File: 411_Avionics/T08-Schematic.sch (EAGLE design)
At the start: 19 parts, among them IC1 BQ24022, U1 USB_In, U3 LSM9DS0

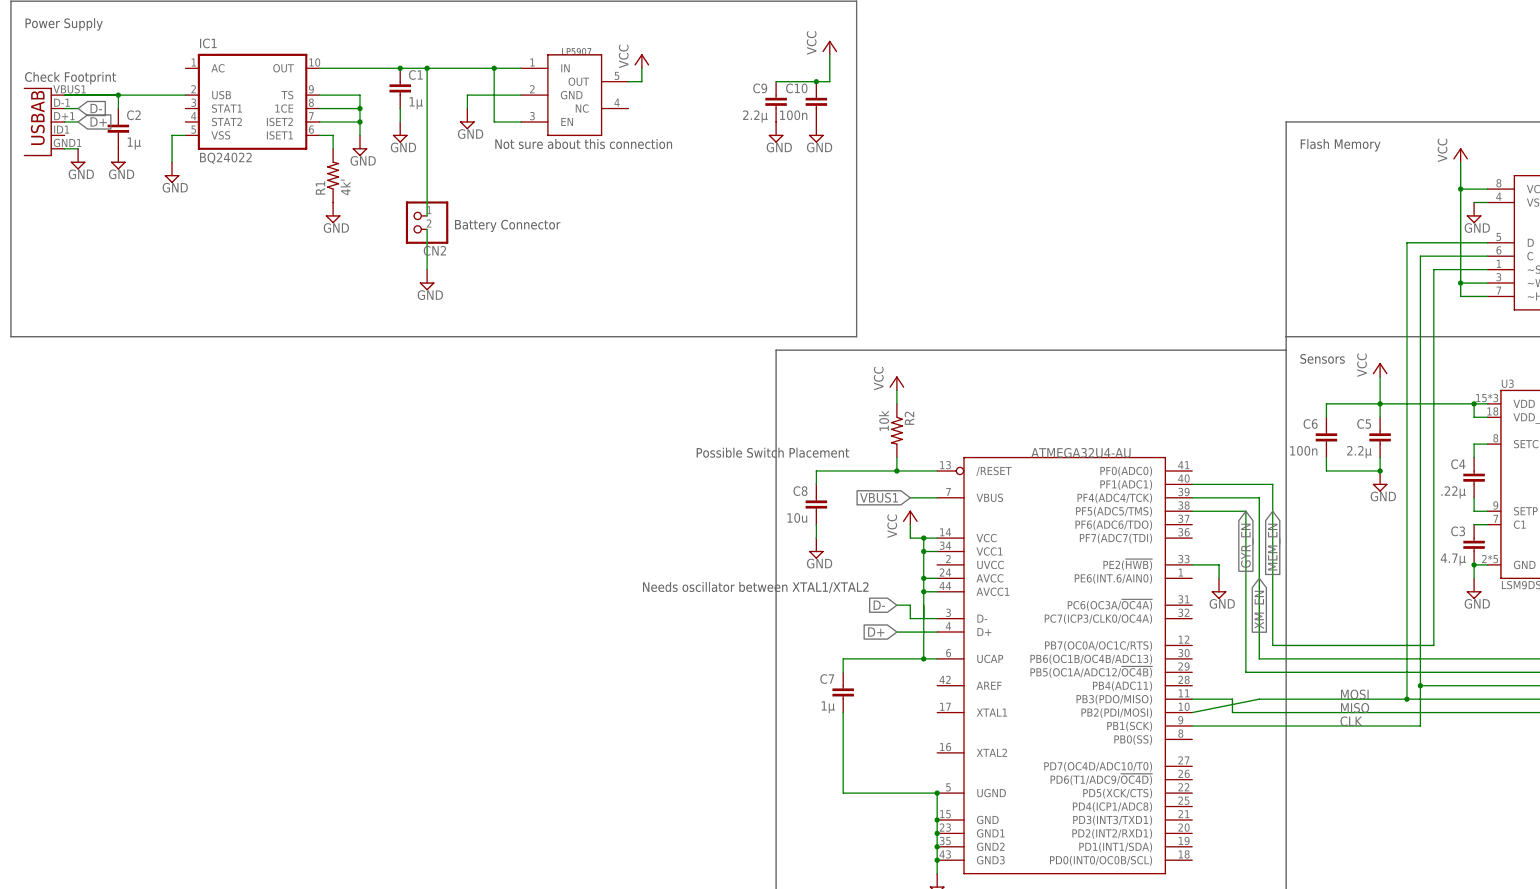
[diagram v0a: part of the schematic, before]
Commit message: Commented changes to be made from design review, removed temp files
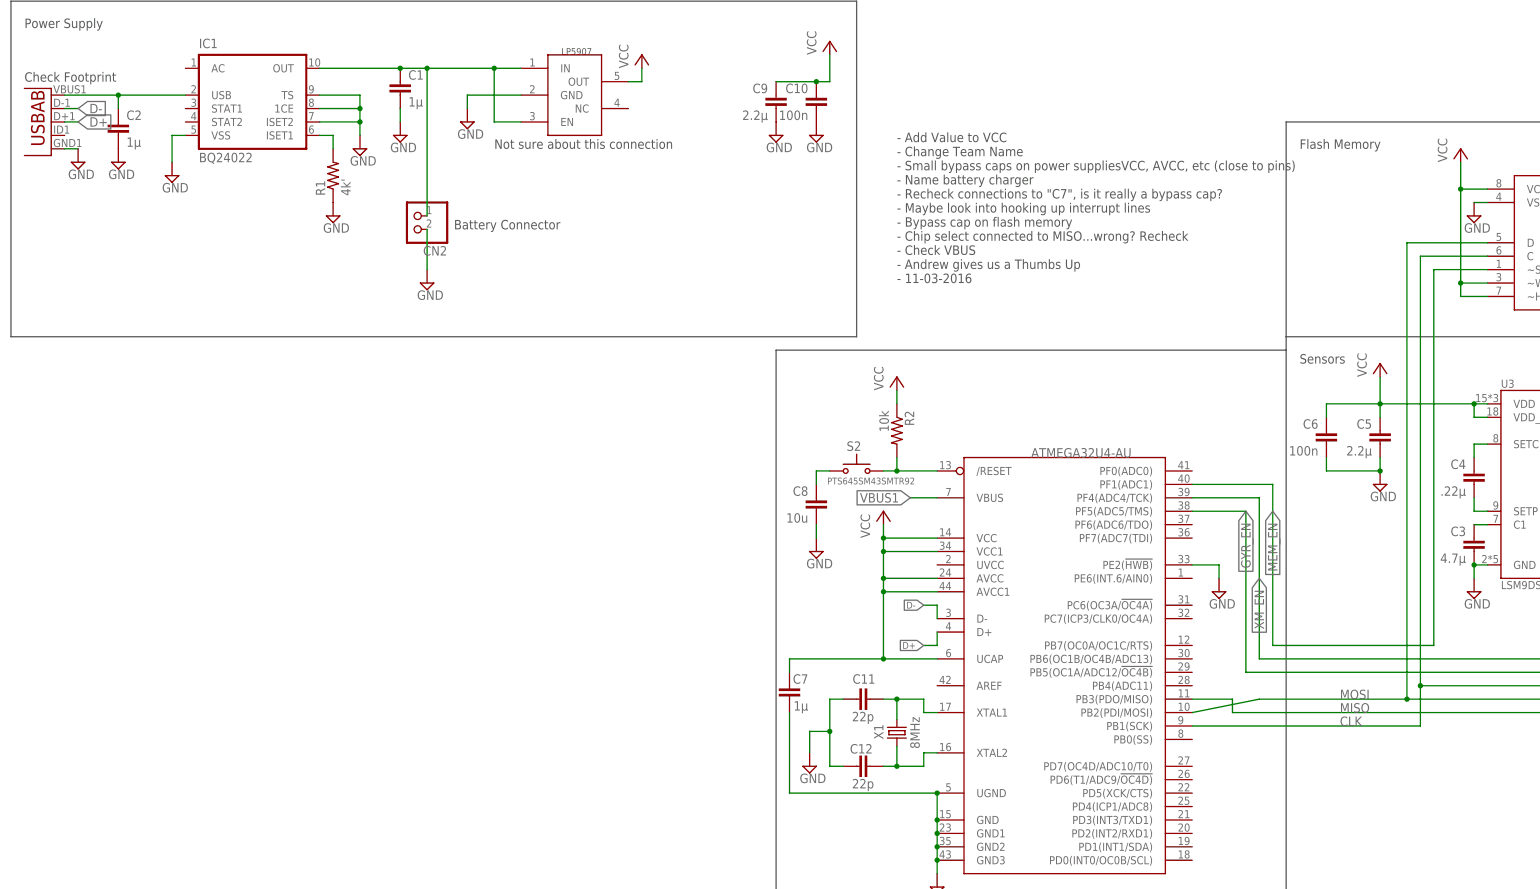
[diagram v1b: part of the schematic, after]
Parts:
- added C11, C12: 22p, rcl:C-EUC0805
- added S2: PTS645SM43SMTR92, switch-ck:PTS645SSMTR
- added X1: 8MHz, IQD-Frequency-Products:CRYSTALS-NOGND-HC49/4H
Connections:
- new net N$3: R2.2, S2.S, U$3./RESET
- new net N$5: C12.1, U$3.XTAL2, X1.2
- new net N$6: C8.1, S2.P
- net GND: now also C11.2, C12.2
- net N$2: now also C11.1, U$3.XTAL1, X1.1; no longer C8.1, R2.2, U$3./RESET
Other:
- note added: "- Add Value to VCC - Change Team Name - Small bypass caps on power suppliesVCC, AVCC, etc (close to pins) - Name battery charger - Recheck connections to "C7", is it really a bypass cap? - Maybe look into hooking up interrupt lines - Bypass cap on flash memory - Chip select connected to MISO...wrong? Recheck - Check VBUS - Andrew gives us a Thumbs Up - 11-03-2016"
- note removed: "Needs oscillator between XTAL1/XTAL2"
- note removed: "Possible Switch Placement"
- moved on the sheet: C7

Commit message: Added more design review notes
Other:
- note added: "Add user power switch Add comparator for enable line Add second LDO for sensor"
- note added: "NEEDS RGB LED ON GPIO BECAUSE OF REASONS"
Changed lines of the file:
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@@
 - Andrew gives us a Thumbs Up
 - 11-03-2016</text>
+<text x="111.76" y="228.6" size="1.778" layer="97">Add user power switch
+Add comparator for enable line
+Add second LDO for sensor</text>
+<text x="187.96" y="86.36" size="1.778" layer="97">NEEDS RGB LED ON GPIO BECAUSE OF REASONS</text>
 </plain>
 <instances>

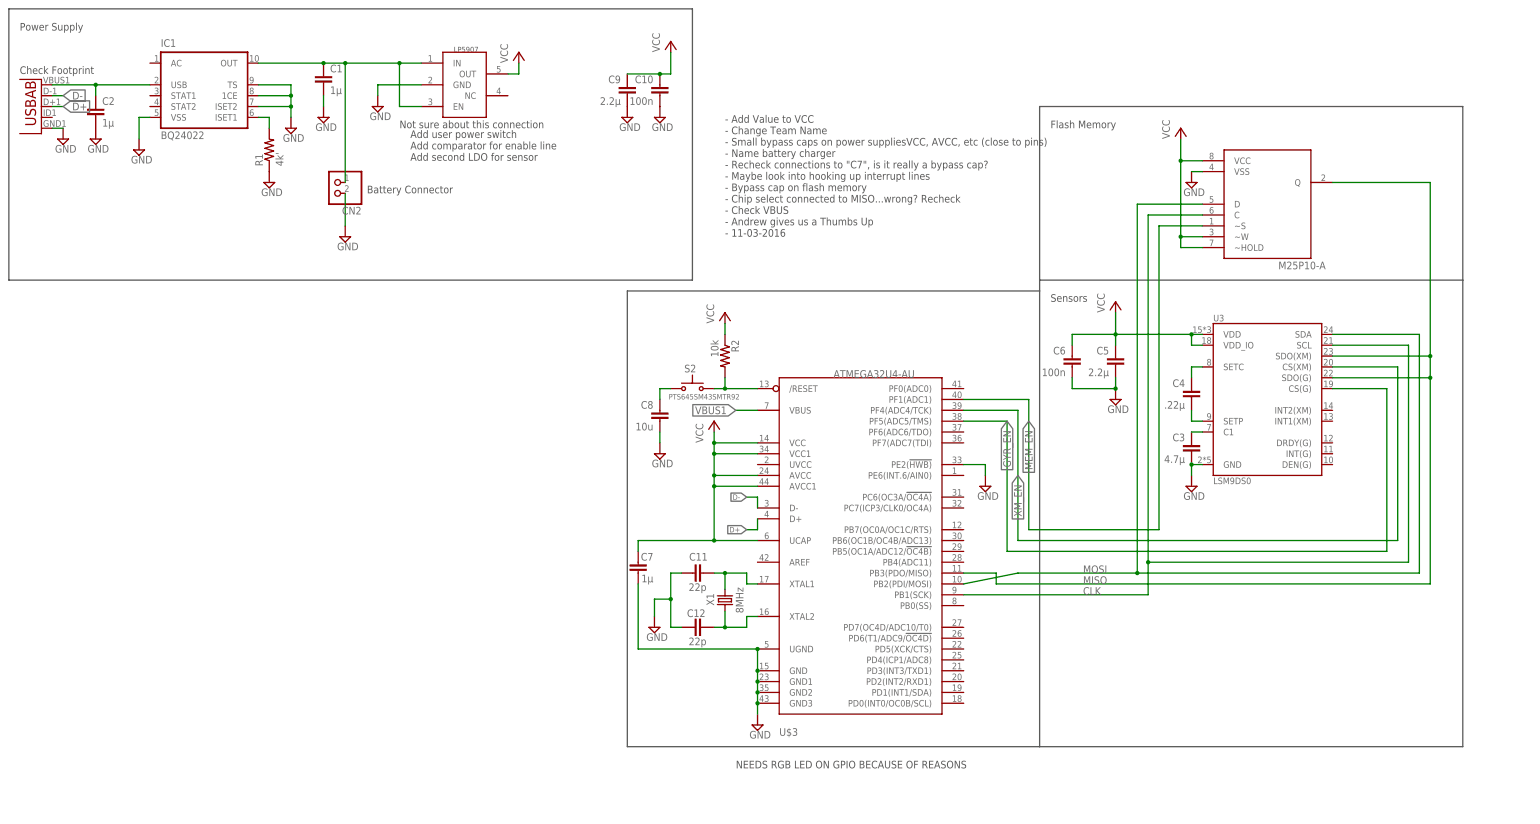
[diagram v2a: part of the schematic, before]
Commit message: Started library of custom footprints. LTC1998 comparator for undervoltage protection. User power switch.
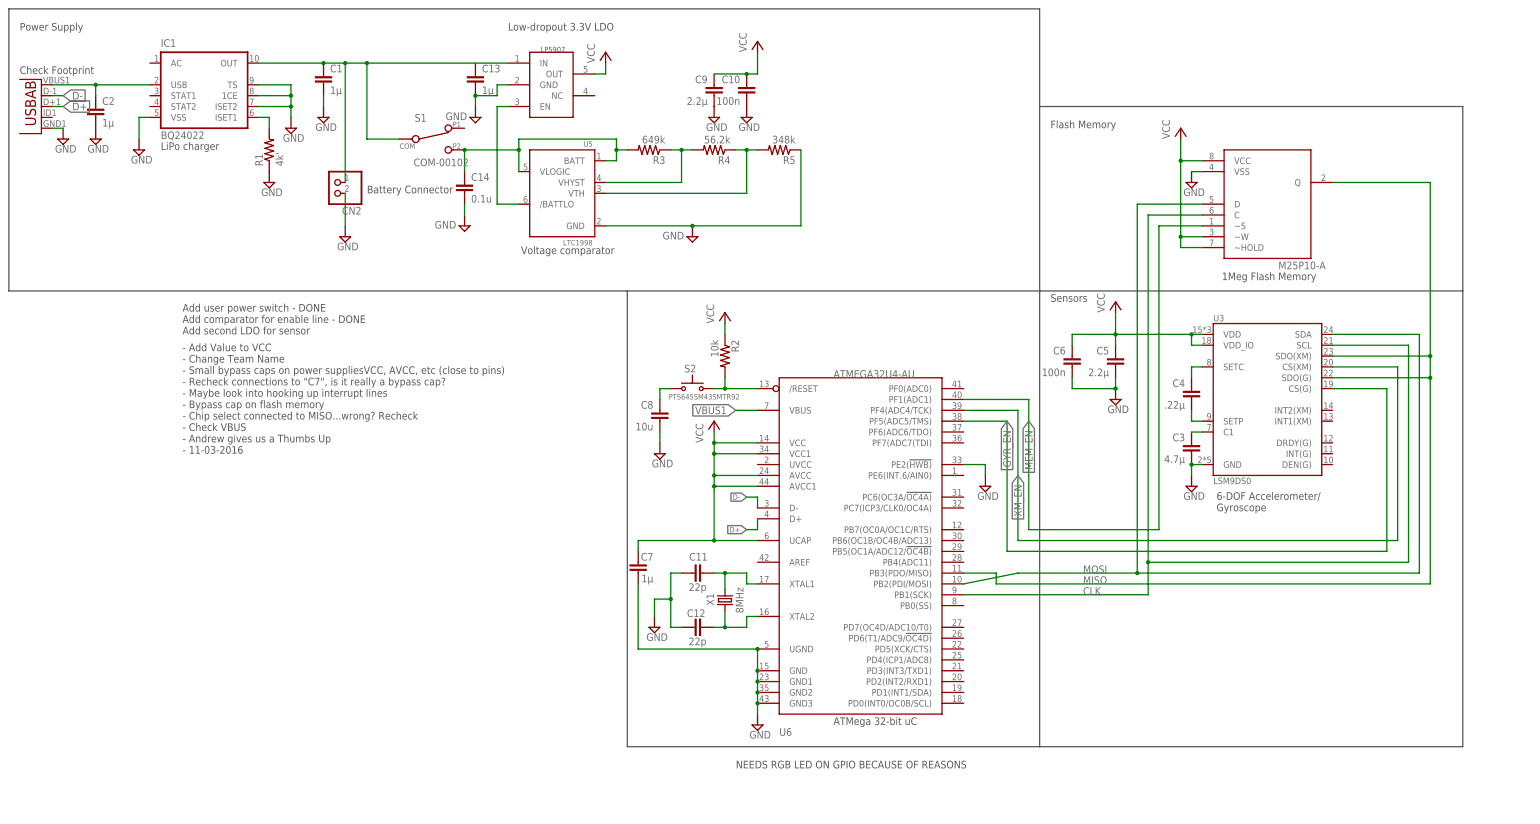
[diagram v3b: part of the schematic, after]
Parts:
- added C13: 1µ, rcl:C-EU050-025X075
- added C14: 0.1u, rcl:C-EU050-025X075
- added R3: 649k, rcl:R-US_R0805
- added R4: 56.2k, rcl:R-US_R0805
- added R5: 348k, rcl:R-US_R0805
- added S1: COM-00102, tinyav-lib:COM-00102
- added U5: LTC1998, tinyav-lib:LTC1998
- renumbered U$1 to U2, U$3 to U6
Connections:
- removed net N$17: C1.1, CN2.2, IC1G$1.OUT, U$2.EN, U$2.IN
- new net N$12: R3.1, R4.2, U5.VHYST
- new net N$13: C1.1, CN2.2, IC1G$1.OUT, S1.COM, U$2.IN
- new net N$14: R4.1, R5.2, U5.VTH
- new net N$15: C14.1, R3.2, S1.P2, U5.BATT, U5.VLOGIC
- new net N$18: U$2.EN, U5./BATTLO
- new net N$7: C13.2, U$2.GND
- net GND: now also C14.2, R5.1, U5.GND; no longer U$2.GND
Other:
- note added: "- Add Value to VCC - Change Team Name - Small bypass caps on power suppliesVCC, AVCC, etc (close to pins) - Recheck connections to "C7", is it really a bypass cap? - Maybe look into hooking up interrupt lines - Bypass cap on flash memory - Chip select connected to MISO...wrong? Recheck - Check VBUS - Andrew gives us a Thumbs Up - 11-03-2016"
- note added: "1Meg Flash Memory"
- note added: "6-DOF Accelerometer/ Gyroscope"
- note added: "ATMega 32-bit uC"
- note added: "Add user power switch - DONE Add comparator for enable line - DONE Add second LDO for sensor"
- note added: "LiPo charger"
- note added: "Low-dropout 3.3V LDO"
- note added: "Voltage comparator"
- note removed: "- Add Value to VCC - Change Team Name - Small bypass caps on power suppliesVCC, AVCC, etc (close to pins) - Name battery charger - Recheck connections to "C7", is it really a bypass cap? - Maybe look into hooking up interrupt lines - Bypass cap on flash memory - Chip select connected to MISO...wrong? Recheck - Check VBUS - Andrew gives us a Thumbs Up - 11-03-2016"
- note removed: "Add user power switch Add comparator for enable line Add second LDO for sensor"
- note removed: "Not sure about this connection"
- moved on the sheet: C10, C9

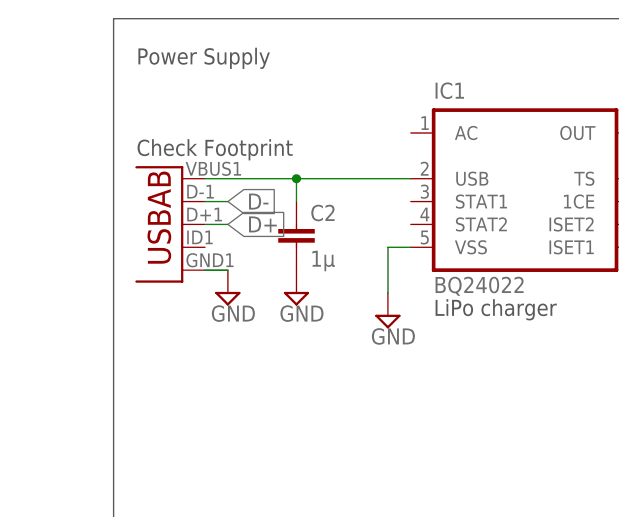
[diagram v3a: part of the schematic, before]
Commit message: Changed to micro-USB B connector from SparkFun library
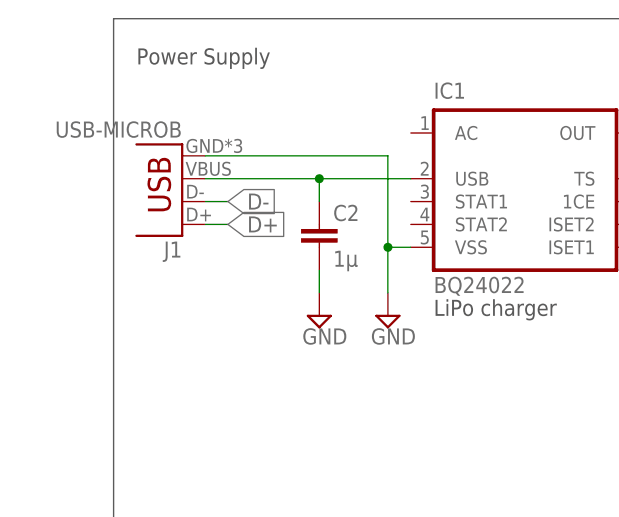
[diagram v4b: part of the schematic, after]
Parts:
- removed U1: USB_In, MicroUSB:USB""
- added J1: USB-MICROB, SparkFun-Connectors:USB-MICROB
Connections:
- net D+: now also J1.D+; no longer U1.D+
- net D-: now also J1.D-; no longer U1.D-
- net GND: now also J1.GND; no longer U1.GND
- net N$1: now also J1.VBUS; no longer U1.VBUS
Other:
- note removed: "Check Footprint"
- moved on the sheet: C2
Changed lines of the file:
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@@
 <layer number="112" name="tSilk" color="7" fill="1" visible="yes" active="yes"/>
 <layer number="113" name="ReferenceLS" color="7" fill="1" visible="no" active="no"/>
+<layer number="114" name="Badge_Outline" color="7" fill="1" visible="yes" active="yes"/>
+<layer number="115" name="ReferenceISLANDS" color="7" fill="1" visible="yes" active="yes"/>
 <layer number="116" name="Patch_BOT" color="9" fill="4" visible="yes" active="yes"/>
 <layer number="118" name="Rect_Pads" color="7" fill="1" visible="no" active="no"/>
@@
 <part name="SUPPLY4" library="supply2" deviceset="GND" device=""/>
 <part name="SUPPLY1" library="supply2" deviceset="GND" device=""/>
-<part name="U1" library="MicroUSB" deviceset="USB" device="&quot;&quot;" value="USB_In"/>
-<part name="SUPPLY6" library="supply2" deviceset="GND" device=""/>
 <part name="R1" library="rcl" deviceset="R-US_" device="0309/12" value="4k'"/>
 <part name="SUPPLY7" library="supply2" deviceset="GND" device=""/>
@@
 <part name="C14" library="rcl" deviceset="C-EU" device="050-025X075" value="0.1u"/>
 <part name="SUPPLY19" library="supply2" deviceset="GND" device=""/>
+<part name="J1" library="SparkFun-Connectors" deviceset="USB" device="-MICROB"/>
 </parts>
 <sheets>
 <sheet>
 <plain>
-<text x="20.32" y="248.92" size="1.778" layer="97">Check Footprint</text>
 <text x="419.1" y="7.366" size="2.54" layer="97">A</text>
 <text x="360.68" y="10.16" size="2.54" layer="97">00000001</text>
@@
 <instance part="IC1" gate="G$1" x="63.5" y="246.38"/>
 <instance part="C1" gate="G$1" x="91.44" y="248.92"/>
-<instance part="C2" gate="G$1" x="38.1" y="241.3"/>
-<instance part="SUPPLY3" gate="GND" x="38.1" y="233.68"/>
+<instance part="C2" gate="G$1" x="40.64" y="241.3"/>
+<instance part="SUPPLY3" gate="GND" x="40.64" y="231.14"/>
 <instance part="SUPPLY4" gate="GND" x="48.26" y="231.14"/>
 <instance part="SUPPLY1" gate="GND" x="83.82" y="236.22"/>
-<instance part="U1" gate="G$1" x="22.86" y="241.3" rot="R180"/>
-<instance part="SUPPLY6" gate="GND" x="30.48" y="233.68"/>
 <instance part="R1" gate="G$1" x="78.74" y="231.14" rot="R90"/>
 <instance part="SUPPLY7" gate="GND" x="78.74" y="223.52"/>
@@
 <attribute name="VALUE" x="117.475" y="212.725" size="1.778" layer="96"/>
 </instance>
+<instance part="J1" gate="G$1" x="25.4" y="248.92" rot="R180"/>
 </instances>
 <busses>
@@
 <pinref part="C2" gate="G$1" pin="2"/>
 <pinref part="SUPPLY3" gate="GND" pin="GND"/>
+<wire x1="40.64" y1="233.68" x2="40.64" y2="236.22" width="0.1524" layer="91"/>
 </segment>
 <segment>
@@
 <pinref part="SUPPLY4" gate="GND" pin="GND"/>
 <wire x1="48.26" y1="238.76" x2="48.26" y2="233.68" width="0.1524" layer="91"/>
+<wire x1="27.94" y1="248.92" x2="48.26" y2="248.92" width="0.1524" layer="91"/>
+<wire x1="48.26" y1="248.92" x2="48.26" y2="238.76" width="0.1524" layer="91"/>
+<junction x="48.26" y="238.76"/>
+<pinref part="J1" gate="G$1" pin="GND"/>
 </segment>
 <segment>
@@
 <wire x1="76.2" y1="241.3" x2="83.82" y2="241.3" width="0.1524" layer="91"/>
 <junction x="83.82" y="241.3"/>
-</segment>
-<segment>
-<pinref part="U1" gate="G$1" pin="GND"/>
-<pinref part="SUPPLY6" gate="GND" pin="GND"/>
-<wire x1="30.48" y1="236.22" x2="27.94" y2="236.22" width="0.1524" layer="91"/>
 </segment>
 <segment>
@@
 <pinref part="IC1" gate="G$1" pin="USB"/>
 <pinref part="C2" gate="G$1" pin="1"/>
-<wire x1="38.1" y1="246.38" x2="50.8" y2="246.38" width="0.1524" layer="91"/>
-<wire x1="38.1" y1="243.84" x2="38.1" y2="246.38" width="0.1524" layer="91"/>
-<pinref part="U1" gate="G$1" pin="VBUS"/>
-<wire x1="38.1" y1="246.38" x2="27.94" y2="246.38" width="0.1524" layer="91"/>
-<junction x="38.1" y="246.38"/>
+<wire x1="40.64" y1="246.38" x2="50.8" y2="246.38" width="0.1524" layer="91"/>
+<wire x1="40.64" y1="243.84" x2="40.64" y2="246.38" width="0.1524" layer="91"/>
+<wire x1="40.64" y1="246.38" x2="27.94" y2="246.38" width="0.1524" layer="91"/>
+<junction x="40.64" y="246.38"/>
+<pinref part="J1" gate="G$1" pin="VBUS"/>
 </segment>
 </net>
 <net name="D-" class="0">
 <segment>
-<pinref part="U1" gate="G$1" pin="D-"/>
 <wire x1="27.94" y1="243.84" x2="30.48" y2="243.84" width="0.1524" layer="91"/>
 <label x="30.48" y="243.84" size="1.778" layer="95" xref="yes"/>
+<pinref part="J1" gate="G$1" pin="D-"/>
 </segment>
 <segment>
@@
 <net name="D+" class="0">
 <segment>
-<pinref part="U1" gate="G$1" pin="D+"/>
 <wire x1="27.94" y1="241.3" x2="30.48" y2="241.3" width="0.1524" layer="91"/>
 <label x="30.48" y="241.3" size="1.778" layer="95" xref="yes"/>
-</segment>
-<segment>
+<pinref part="J1" gate="G$1" pin="D+"/>
+</segment>
+<segment>
